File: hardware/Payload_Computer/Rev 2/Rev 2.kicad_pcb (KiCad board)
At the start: 2 copper layers, 101.6 x 101.6 mm, 1 part, among them U201 Teensy3.2

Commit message: Added Voltage Regulator
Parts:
- added H101: Center_Hole, Rev 2:Center_hole, F.Cu at (162.2, 92.0)
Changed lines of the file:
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@@
     (tracks 0)
     (zones 0)
-    (modules 1)
+    (modules 2)
     (nets 37)
   )
@@
     (mod_text_size 1 1)
     (mod_text_width 0.15)
-    (pad_size 1.524 1.524)
-    (pad_drill 0.762)
+    (pad_size 13 13)
+    (pad_drill 12.7)
     (pad_to_mask_clearance 0)
     (aux_axis_origin 0 0)
-    (visible_elements FFFFFF7F)
+    (visible_elements 7FFFFFFF)
     (pcbplotparams
       (layerselection 0x010fc_ffffffff)
@@
     (add_net "Net-(U201-Pad9)")
   )
+  (module "Rev 2:Center_hole" (layer F.Cu)
+    (at 162.2 92)
+    (fp_text reference H101 (at 0.09 -14.19) (layer F.SilkS)
+      (effects (font (size 1 1) (thickness 0.15)))
+    )
+    (fp_text value Center_Hole (at -0.05 -12.63) (layer F.Fab)
+      (effects (font (size 1 1) (thickness 0.15)))
+    )
+    (pad 1 thru_hole circle (at 0 0.8) (size 13 13) (drill 12.7) (layers *.Cu *.Mask))
+  )
   (module teensy:Teensy30_31_32_LC (layer F.Cu)
     (at 163.5 61.4)
@@
       (effects (font (size 1 1) (thickness 0.15)))
     )
+    (fp_poly (pts (xy 4.826 2.921) (xy 4.572 2.667) (xy 4.953 2.413) (xy 5.207 2.667)) (layer F.SilkS) (width 0.1))
+    (fp_poly (pts (xy 3.81 3.683) (xy 3.556 3.429) (xy 3.937 3.175) (xy 4.191 3.429)) (layer F.SilkS) (width 0.1))
+    (fp_poly (pts (xy 4.572 4.445) (xy 4.318 4.191) (xy 4.699 3.937) (xy 4.953 4.191)) (layer F.SilkS) (width 0.1))
+    (fp_poly (pts (xy 4.445 2.54) (xy 4.191 2.286) (xy 4.572 2.032) (xy 4.826 2.286)) (layer F.SilkS) (width 0.1))
+    (fp_poly (pts (xy 4.191 4.064) (xy 3.937 3.81) (xy 4.318 3.556) (xy 4.572 3.81)) (layer F.SilkS) (width 0.1))
+    (fp_poly (pts (xy 4.953 2.159) (xy 4.699 1.905) (xy 5.08 1.651) (xy 5.334 1.905)) (layer F.SilkS) (width 0.1))
+    (fp_poly (pts (xy 4.318 3.302) (xy 4.064 3.048) (xy 4.445 2.794) (xy 4.699 3.048)) (layer F.SilkS) (width 0.1))
+    (fp_poly (pts (xy 3.937 2.921) (xy 3.683 2.667) (xy 4.064 2.413) (xy 4.318 2.667)) (layer F.SilkS) (width 0.1))
+    (fp_line (start -17.78 8.89) (end -17.78 -8.89) (layer F.SilkS) (width 0.15))
+    (fp_line (start 17.78 8.89) (end -17.78 8.89) (layer F.SilkS) (width 0.15))
+    (fp_line (start 17.78 -8.89) (end 17.78 8.89) (layer F.SilkS) (width 0.15))
+    (fp_line (start -17.78 -8.89) (end 17.78 -8.89) (layer F.SilkS) (width 0.15))
+    (fp_line (start 8.89 5.08) (end 0 5.08) (layer F.SilkS) (width 0.15))
+    (fp_line (start 8.89 -5.08) (end 0 -5.08) (layer F.SilkS) (width 0.15))
+    (fp_line (start 0 -5.08) (end 0 5.08) (layer F.SilkS) (width 0.15))
+    (fp_line (start 8.89 5.08) (end 8.89 -5.08) (layer F.SilkS) (width 0.15))
+    (fp_line (start 12.7 -2.54) (end 15.24 -2.54) (layer F.SilkS) (width 0.15))
+    (fp_line (start 12.7 2.54) (end 12.7 -2.54) (layer F.SilkS) (width 0.15))
+    (fp_line (start 15.24 2.54) (end 12.7 2.54) (layer F.SilkS) (width 0.15))
+    (fp_line (start 15.24 -2.54) (end 15.24 2.54) (layer F.SilkS) (width 0.15))
+    (fp_line (start -11.43 2.54) (end -11.43 5.08) (layer F.SilkS) (width 0.15))
+    (fp_line (start -8.89 2.54) (end -11.43 2.54) (layer F.SilkS) (width 0.15))
+    (fp_line (start -8.89 5.08) (end -8.89 2.54) (layer F.SilkS) (width 0.15))
+    (fp_line (start -11.43 5.08) (end -8.89 5.08) (layer F.SilkS) (width 0.15))
+    (fp_line (start -12.7 3.81) (end -17.78 3.81) (layer F.SilkS) (width 0.15))
+    (fp_line (start -12.7 -3.81) (end -17.78 -3.81) (layer F.SilkS) (width 0.15))
+    (fp_line (start -12.7 3.81) (end -12.7 -3.81) (layer F.SilkS) (width 0.15))
+    (fp_line (start -6.35 2.54) (end -6.35 5.08) (layer F.SilkS) (width 0.15))
+    (fp_line (start -2.54 2.54) (end -6.35 2.54) (layer F.SilkS) (width 0.15))
+    (fp_line (start -2.54 5.08) (end -2.54 2.54) (layer F.SilkS) (width 0.15))
+    (fp_line (start -6.35 5.08) (end -2.54 5.08) (layer F.SilkS) (width 0.15))
+    (fp_line (start -19.05 -3.81) (end -17.78 -3.81) (layer F.SilkS) (width 0.15))
+    (fp_line (start -19.05 3.81) (end -19.05 -3.81) (layer F.SilkS) (width 0.15))
+    (fp_line (start -17.78 3.81) (end -19.05 3.81) (layer F.SilkS) (width 0.15))
     (fp_text user MK20DX128VLH5 (at 4.445 -1.524) (layer F.SilkS)
       (effects (font (size 0.7 0.7) (thickness 0.15)))
@@
       (effects (font (size 1 1) (thickness 0.15)))
     )
-    (fp_line (start -17.78 3.81) (end -19.05 3.81) (layer F.SilkS) (width 0.15))
-    (fp_line (start -19.05 3.81) (end -19.05 -3.81) (layer F.SilkS) (width 0.15))
-    (fp_line (start -19.05 -3.81) (end -17.78 -3.81) (layer F.SilkS) (width 0.15))
-    (fp_line (start -6.35 5.08) (end -2.54 5.08) (layer F.SilkS) (width 0.15))
-    (fp_line (start -2.54 5.08) (end -2.54 2.54) (layer F.SilkS) (width 0.15))
-    (fp_line (start -2.54 2.54) (end -6.35 2.54) (layer F.SilkS) (width 0.15))
-    (fp_line (start -6.35 2.54) (end -6.35 5.08) (layer F.SilkS) (width 0.15))
-    (fp_line (start -12.7 3.81) (end -12.7 -3.81) (layer F.SilkS) (width 0.15))
-    (fp_line (start -12.7 -3.81) (end -17.78 -3.81) (layer F.SilkS) (width 0.15))
-    (fp_line (start -12.7 3.81) (end -17.78 3.81) (layer F.SilkS) (width 0.15))
-    (fp_line (start -11.43 5.08) (end -8.89 5.08) (layer F.SilkS) (width 0.15))
-    (fp_line (start -8.89 5.08) (end -8.89 2.54) (layer F.SilkS) (width 0.15))
-    (fp_line (start -8.89 2.54) (end -11.43 2.54) (layer F.SilkS) (width 0.15))
-    (fp_line (start -11.43 2.54) (end -11.43 5.08) (layer F.SilkS) (width 0.15))
-    (fp_line (start 15.24 -2.54) (end 15.24 2.54) (layer F.SilkS) (width 0.15))
-    (fp_line (start 15.24 2.54) (end 12.7 2.54) (layer F.SilkS) (width 0.15))
-    (fp_line (start 12.7 2.54) (end 12.7 -2.54) (layer F.SilkS) (width 0.15))
-    (fp_line (start 12.7 -2.54) (end 15.24 -2.54) (layer F.SilkS) (width 0.15))
-    (fp_line (start 8.89 5.08) (end 8.89 -5.08) (layer F.SilkS) (width 0.15))
-    (fp_line (start 0 -5.08) (end 0 5.08) (layer F.SilkS) (width 0.15))
-    (fp_line (start 8.89 -5.08) (end 0 -5.08) (layer F.SilkS) (width 0.15))
-    (fp_line (start 8.89 5.08) (end 0 5.08) (layer F.SilkS) (width 0.15))
-    (fp_line (start -17.78 -8.89) (end 17.78 -8.89) (layer F.SilkS) (width 0.15))
-    (fp_line (start 17.78 -8.89) (end 17.78 8.89) (layer F.SilkS) (width 0.15))
-    (fp_line (start 17.78 8.89) (end -17.78 8.89) (layer F.SilkS) (width 0.15))
-    (fp_line (start -17.78 8.89) (end -17.78 -8.89) (layer F.SilkS) (width 0.15))
-    (fp_poly (pts (xy 3.937 2.921) (xy 3.683 2.667) (xy 4.064 2.413) (xy 4.318 2.667)) (layer F.SilkS) (width 0.1))
-    (fp_poly (pts (xy 4.318 3.302) (xy 4.064 3.048) (xy 4.445 2.794) (xy 4.699 3.048)) (layer F.SilkS) (width 0.1))
-    (fp_poly (pts (xy 4.953 2.159) (xy 4.699 1.905) (xy 5.08 1.651) (xy 5.334 1.905)) (layer F.SilkS) (width 0.1))
-    (fp_poly (pts (xy 4.191 4.064) (xy 3.937 3.81) (xy 4.318 3.556) (xy 4.572 3.81)) (layer F.SilkS) (width 0.1))
-    (fp_poly (pts (xy 4.445 2.54) (xy 4.191 2.286) (xy 4.572 2.032) (xy 4.826 2.286)) (layer F.SilkS) (width 0.1))
-    (fp_poly (pts (xy 4.572 4.445) (xy 4.318 4.191) (xy 4.699 3.937) (xy 4.953 4.191)) (layer F.SilkS) (width 0.1))
-    (fp_poly (pts (xy 3.81 3.683) (xy 3.556 3.429) (xy 3.937 3.175) (xy 4.191 3.429)) (layer F.SilkS) (width 0.1))
-    (fp_poly (pts (xy 4.826 2.921) (xy 4.572 2.667) (xy 4.953 2.413) (xy 5.207 2.667)) (layer F.SilkS) (width 0.1))
     (pad 52 thru_hole circle (at -10.16 0) (size 1.9 1.9) (drill 0.5) (layers *.Cu *.Mask)
       (net 1 "Net-(U201-Pad52)"))

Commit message: Minor Updates
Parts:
- added C301: 10uF, Capacitor_Tantalum_SMD:CP_EIA-6032-20_AVX-F_Pad2.25x2.35mm_HandSolder, F.Cu at (198.7, 79.0)
- added C302: 10uF, Capacitor_Tantalum_SMD:CP_EIA-6032-20_AVX-F_Pad2.25x2.35mm_HandSolder, F.Cu at (198.7, 83.8)
- added U301: MIC29151-5.0WU-TR, footprints:MIC29151-5.0WU-TR, F.Cu at (188.0, 84.4)
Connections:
- U201 pad 33: Net-(U201-Pad33) -> +5V

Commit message: Finished the overbuilt power supply and did some minor routing
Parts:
- added C303: 10uF, Capacitor_Tantalum_SMD:CP_EIA-6032-20_AVX-F_Pad2.25x2.35mm_HandSolder, F.Cu at (121.9, 89.1)
- added C304: 10uF, Capacitor_Tantalum_SMD:CP_EIA-6032-20_AVX-F_Pad2.25x2.35mm_HandSolder, F.Cu at (131.7, 89.1)
- added CR301: B320B-13, footprints-diode:B320B-13, F.Cu at (197.9, 102.5)
- added CR302: B320B-13, footprints-diode:B320B-13, F.Cu at (124.5, 96.1)
- added VR301: LT1963AEST-3.3#PBF, LT1963AEST-3:SOT223, F.Cu at (126.8, 81.2)
- moved C301 17.0 mm to (195.3, 95.7), turned to 180 degrees
- moved C302 13.7 mm to (205.6, 95.7)
- moved U301 13.4 mm to (201.3, 82.2)
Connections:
- net +BATT renamed Net-(C301-Pad1)
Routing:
- net Net-(C301-Pad1): track 0.00 -> 11.1 mm
- net GND: track 0.00 -> 10.4 mm
- net Net-(C303-Pad1): track 0.00 -> 9.92 mm
- net +3V3: track 0.00 -> 4.81 mm
- net +5V: track 0.00 -> 4.37 mm
- added copper zone on B.Cu, net +3V3
- added copper zone on F.Cu, net GND

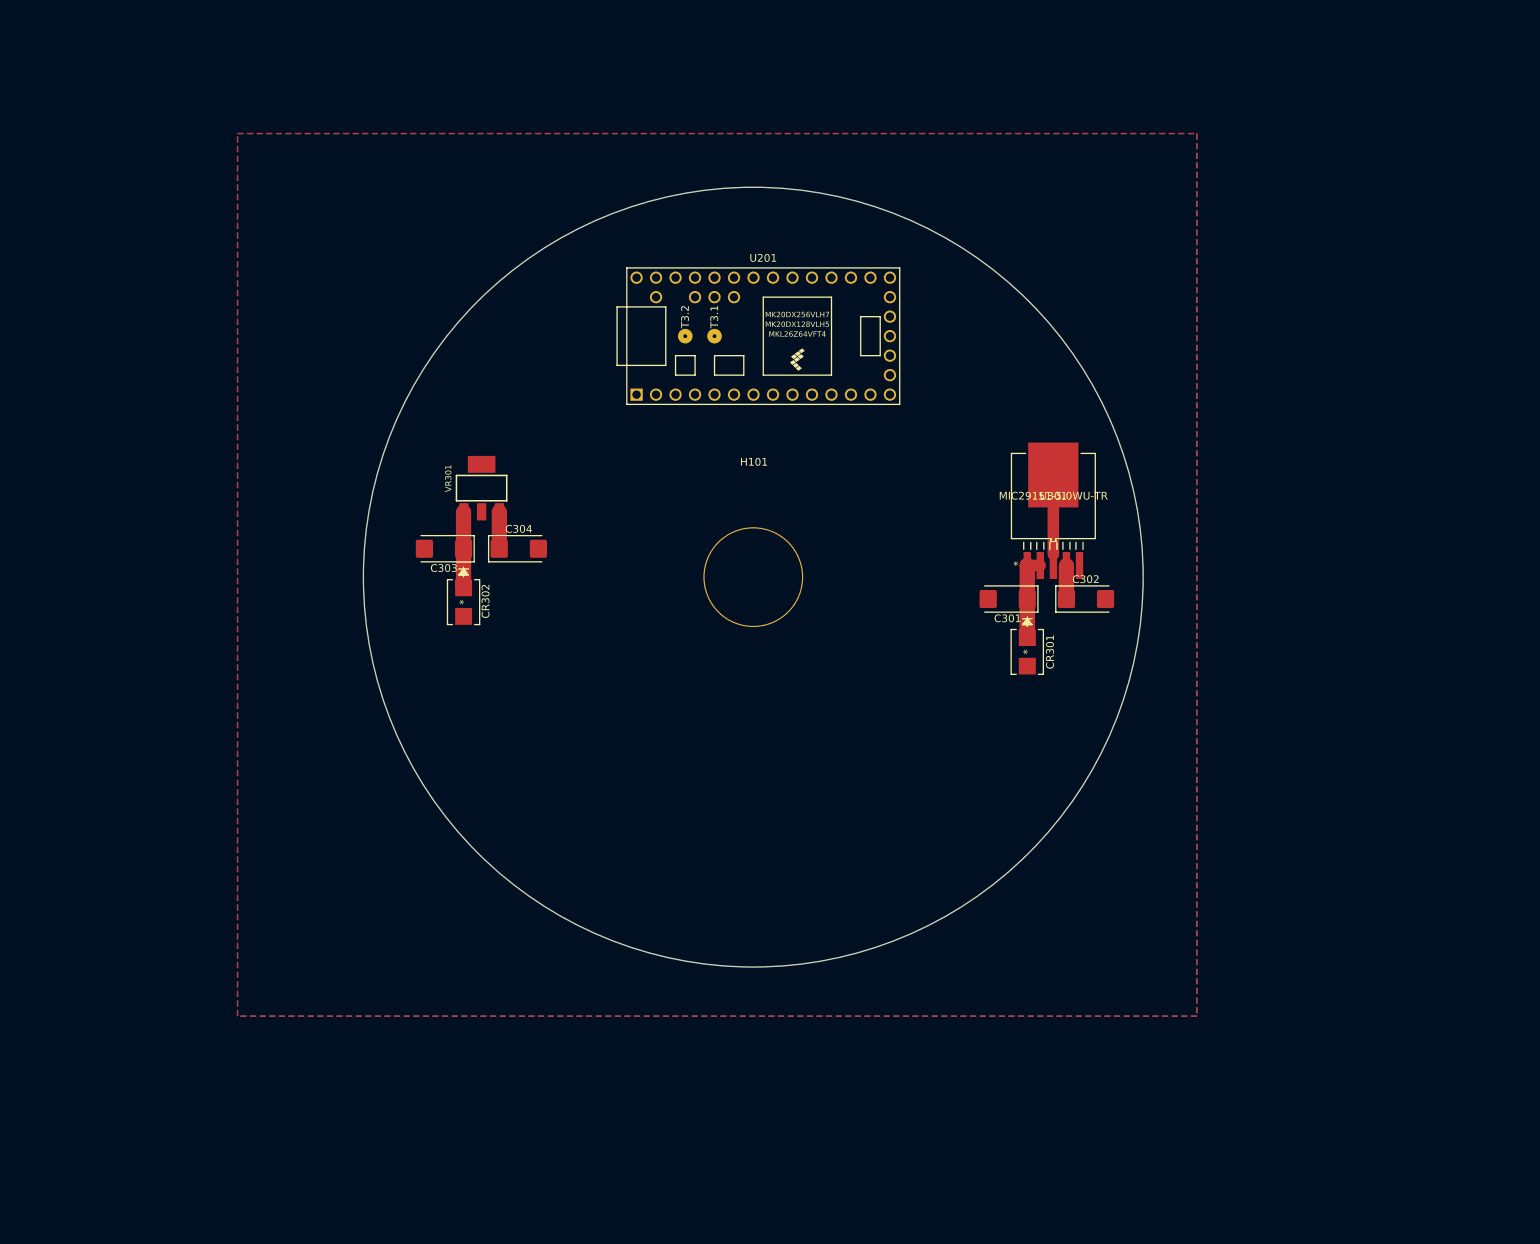
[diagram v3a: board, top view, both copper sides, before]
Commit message: More routing and added BNO055
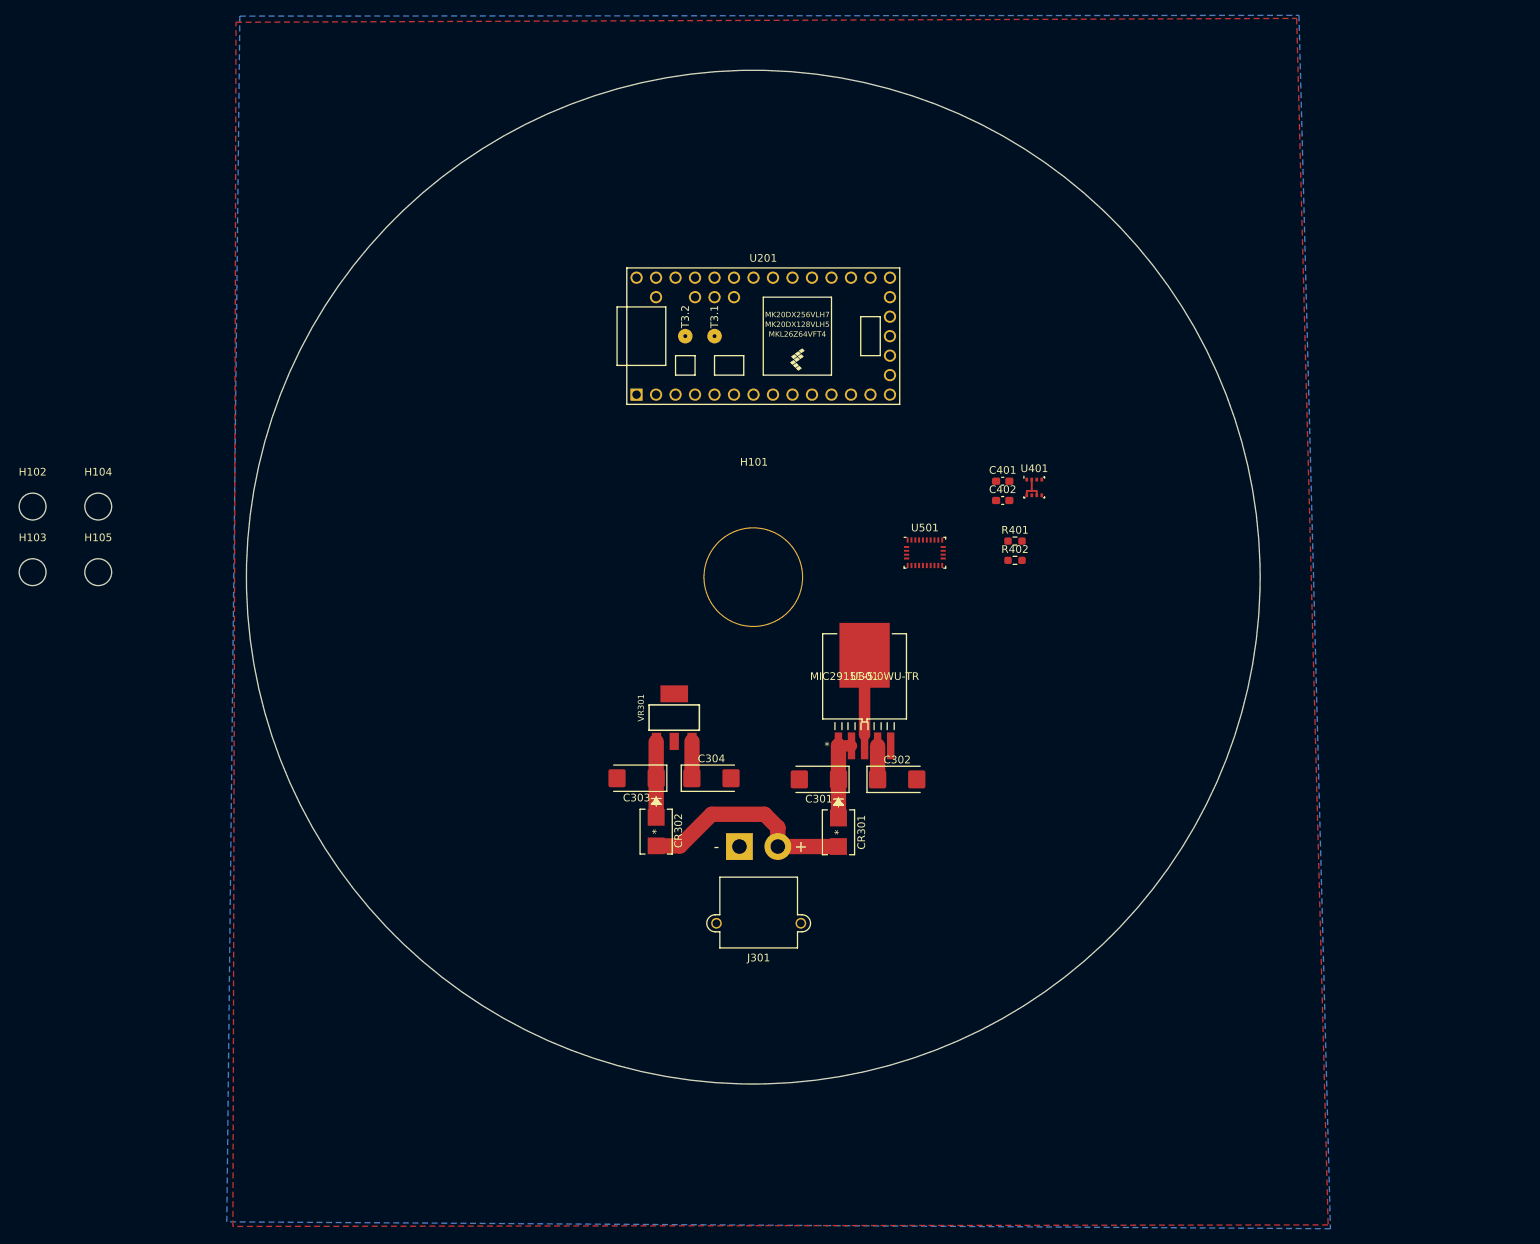
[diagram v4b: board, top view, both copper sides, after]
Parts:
- added C401: 100nF, Capacitor_SMD:C_0603_1608Metric_Pad1.08x0.95mm_HandSolder, F.Cu at (194.7, 80.3)
- added C402: 100nF, Capacitor_SMD:C_0603_1608Metric_Pad1.08x0.95mm_HandSolder, F.Cu at (194.7, 82.8)
- added H102: MountingHole, MountingHole:MountingHole_3.5mm, F.Cu at (68.3, 83.6)
- added H103: MountingHole, MountingHole:MountingHole_3.5mm, F.Cu at (68.3, 92.2)
- added H104: MountingHole, MountingHole:MountingHole_3.5mm, F.Cu at (76.8, 83.6)
- added H105: MountingHole, MountingHole:MountingHole_3.5mm, F.Cu at (76.8, 92.2)
- added J301: Conn_01x02_Female, Connector_AMASS:AMASS_XT30PW-M_1x02_P2.50mm_Horizontal, F.Cu at (160.4, 127.9)
- added R401: 4.7K, Resistor_SMD:R_0603_1608Metric_Pad0.98x0.95mm_HandSolder, F.Cu at (196.3, 88.1)
- added R402: 4.7K, Resistor_SMD:R_0603_1608Metric_Pad0.98x0.95mm_HandSolder, F.Cu at (196.3, 90.6)
- added U401: BME280, Package_LGA:Bosch_LGA-8_2.5x2.5mm_P0.65mm_ClockwisePinNumbering, F.Cu at (198.8, 81.1)
- added U501: BNO055, Package_LGA:LGA-28_5.2x3.8mm_P0.5mm, F.Cu at (184.6, 89.6)
- moved CR302 39.0 mm to (149.6, 126.0)
- moved VR301 39.0 mm to (151.9, 111.1)
- moved C303 39.0 mm to (147.0, 119.0)
- moved C304 39.0 mm to (156.8, 119.0)
- moved C302 34.0 mm to (180.9, 119.2)
- moved U301 34.0 mm to (176.7, 105.7)
- moved C301 34.0 mm to (170.8, 119.2)
- moved CR301 34.0 mm to (173.3, 126.0)
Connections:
- U201 pad 25: Net-(U201-Pad25) -> /SCL
- U201 pad 26: Net-(U201-Pad26) -> /SDA
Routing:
- net +BATT: track 0.00 -> 28.6 mm
- net +3V3: track 4.81 -> 8.65 mm
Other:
- board size 101.6 x 101.6 mm -> 132.1 x 132.1 mm

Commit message: Did some stuff
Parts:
- added U601: 503182-1852, SD_CARD:503182-1852, F.Cu at (220.3, 102.6)
- added U701: W25N01GVZEIG, FLASH:W25N01GVZEIG, F.Cu at (256.1, 105.2)
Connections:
- U501 pad 11: Net-(U501-Pad11) -> Net-(R503-Pad2)
- U501 pad 17: Net-(U501-Pad17) -> GND
- U501 pad 18: Net-(U501-Pad18) -> GND
- U501 pad 19: Net-(U501-Pad19) -> /SCL
- U501 pad 20: Net-(U501-Pad20) -> /SDA
- U501 pad 4: Net-(U501-Pad4) -> Net-(R503-Pad2)
- U501 pad 5: Net-(U501-Pad5) -> GND
- U501 pad 6: Net-(U501-Pad6) -> GND

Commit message: Finished some routing
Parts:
- added C501: 120nF, Capacitor_SMD:C_0603_1608Metric_Pad1.08x0.95mm_HandSolder, F.Cu at (158.4, 75.4)
- added C502: 1uF, Capacitor_SMD:C_0603_1608Metric_Pad1.08x0.95mm_HandSolder, F.Cu at (161.9, 77.0)
- added C503: 22pF, Capacitor_SMD:C_0603_1608Metric_Pad1.08x0.95mm_HandSolder, F.Cu at (164.2, 69.4)
- added C504: 22pF, Capacitor_SMD:C_0603_1608Metric_Pad1.08x0.95mm_HandSolder, F.Cu at (160.6, 69.4)
- added C601: 100nF, Capacitor_SMD:C_0603_1608Metric_Pad1.08x0.95mm_HandSolder, F.Cu at (138.3, 64.9)
- added C701: 100nF, Capacitor_SMD:C_0603_1608Metric_Pad1.08x0.95mm_HandSolder, F.Cu at (150.3, 68.2)
- added R503: 10k, Resistor_SMD:R_0603_1608Metric_Pad0.98x0.95mm_HandSolder, F.Cu at (159.3, 72.7)
- added Y501: 32.768KHz, footprints:crystal, F.Cu at (163.1, 67.7)
- moved U701 109.6 mm to (151.3, 73.2), turned to 90 degrees
- moved U601 97.7 mm to (127.0, 73.8), turned to 90 degrees
- moved C301 38.3 mm to (132.8, 113.8)
- moved CR301 38.3 mm to (135.4, 120.6)
- moved C302 38.3 mm to (143.1, 113.8)
- moved U301 38.3 mm to (138.8, 100.3)
- moved R402 33.0 mm to (171.9, 68.4)
- moved U401 28.2 mm to (172.0, 72.4)
- moved U501 27.1 mm to (163.5, 72.6)
- moved R401 26.8 mm to (174.6, 72.3), turned to 90 degrees
- moved C401 26.5 mm to (169.4, 72.4), turned to 270 degrees
- moved C402 23.8 mm to (172.3, 75.0)
- moved U201 5.58 mm to (162.2, 56.0)
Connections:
- U201 pad 13: Net-(U201-Pad13) -> /MOSI
- U201 pad 14: Net-(U201-Pad14) -> /MISO
- U201 pad 20: Net-(U201-Pad20) -> /SCK
- U201 pad 21: Net-(U201-Pad21) -> /CS_SD
- U201 pad 22: Net-(U201-Pad22) -> /CS_FLASH
- U701 pad 2: Net-(U701-Pad2) -> /MISO
- U701 pad 5: Net-(U701-Pad5) -> /MOSI
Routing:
- net /SCK: track 0.00 -> 59.1 mm, vias 0 -> 2
- net /MISO: track 0.00 -> 53.9 mm, vias 0 -> 1
- net /CS_SD: track 0.00 -> 52.5 mm, vias 0 -> 1
- net /MOSI: track 0.00 -> 48.3 mm, vias 0 -> 2
- net /CS_FLASH: track 0.00 -> 43.7 mm, vias 0 -> 3
- net /SCL: track 0.00 -> 39.7 mm, vias 0 -> 2
- net +3V3: track 8.65 -> 46.9 mm, vias 0 -> 6
- net /SDA: track 0.00 -> 37.1 mm, vias 0 -> 2
- net GND: track 10.4 -> 34.5 mm
- net +BATT: track 28.6 -> 37.1 mm
- net Net-(R503-Pad2): track 0.00 -> 5.62 mm
- net Net-(U201-Pad52): track 0.00 -> 3.81 mm
- net Net-(C504-Pad1): track 0.00 -> 3.63 mm
- net Net-(C503-Pad2): track 0.00 -> 3.58 mm
- net Net-(C502-Pad1): track 0.00 -> 2.72 mm
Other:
- outline, holes or cut-outs redrawn
